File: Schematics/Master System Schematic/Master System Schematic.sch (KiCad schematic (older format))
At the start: 39 parts, among them J1 ChargerHVConn, J2 ChargerLVConn, J3 GND, J5 TS+, J6 TS-, M1 Cooling Pump, SW1 SideMounted (BRB), SW10 SMD, SW11 BRAKE_SWITCH, SW12 SW_SPST_Pressure, SW13 SW_SPST_Pressure, SW14 TOGGLE_SWITCH, SW2 SideMounted (BRB), SW3 GLVMS, SW4 Brake Over-Travel Switch, SW5 Latching Circuit Reset, SW6 Cockpit Shutdown (BRB), SW7 TSMS, SW8 SMD, SW9 HVD, U1 FuseBox_PSZACCEPS052H, U2 Bender_Isometer_IR155-3204, U3 RinehartPM100DX_MotorControll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, U4 Emrax228HV_Motor

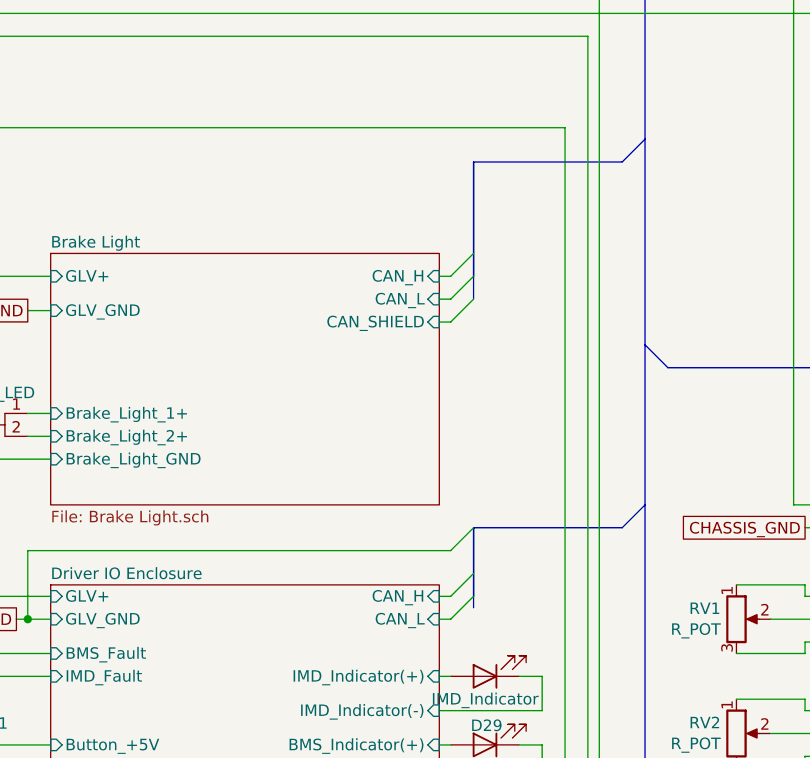
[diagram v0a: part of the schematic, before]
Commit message: Added CAN Shield Label
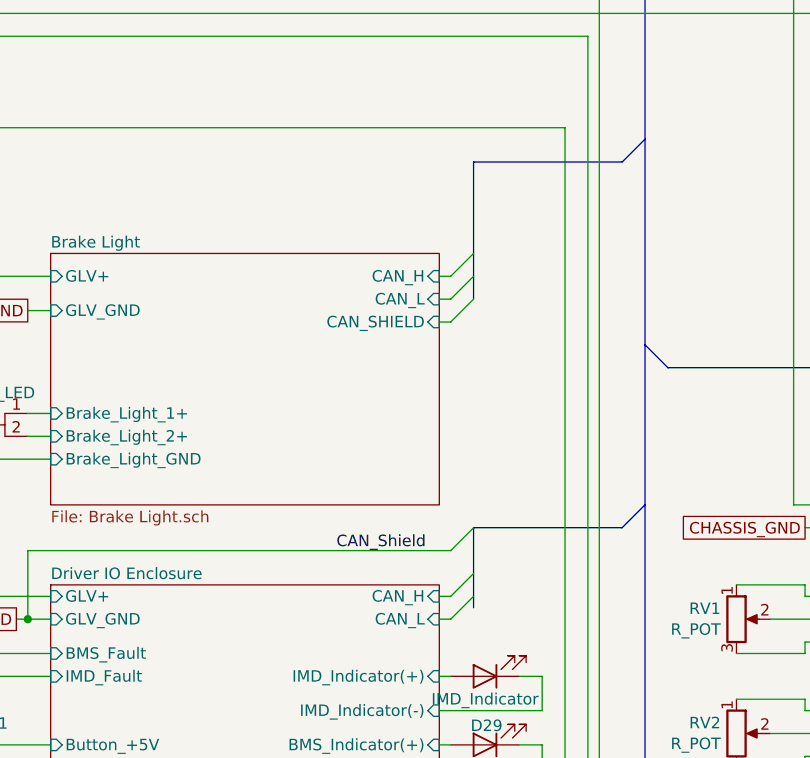
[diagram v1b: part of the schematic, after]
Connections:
- new net: U1.6, U3.23 (CANB_H), U3.8 (Reverse_Enable_Switch)
- new net: U3.~ (TS-), U4.~ (AC3) (x2)
- now unconnected: U3.23 (CANB_H), U3.8 (Reverse_Enable_Switch)
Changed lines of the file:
@@
 EESchema Schematic File Version 4
+LIBS:Master System Schematic-cache
 EELAYER 30 0
 EELAYER END
@@
 Wire Wire Line
 	7900 9400 8200 9400
-Wire Bus Line
-	11300 1650 11300 2150
+Text Label 10700 3350 0    50   ~ 0
+CAN_Shield
+Wire Bus Line
+	14550 2550 14550 3150
+Wire Bus Line
+	11650 6600 11650 6800
 Wire Bus Line
 	11300 3250 11300 3600
 Wire Bus Line
-	14550 2550 14550 3150
-Wire Bus Line
-	11650 6600 11650 6800
-Wire Bus Line
-	11300 3250 11300 3550
-Wire Bus Line
 	11300 1650 11300 2250

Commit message: Rotated first section of GLV
Increased sheet size (May still downsize back to C)
Moved GLV from CHS GND to fusebox
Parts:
- removed SW1: SideMounted (BRB), symbol Switch:SW_Push_Open
- added SW3: Side BRB, symbol Switch:SW_Push_Open
- added U1: FuseBox_PSZACCEPS052H, symbol NER:FuseBox_PSZACCEPS052H
- BT1: value 12V GLV Battery -> GLV Battery; Voltage (none) -> 12V
- CB1: value GLV Main Breaker [30A] -> GLV Main Breaker; Current (none) -> 30A
- SW2: value SideMounted (BRB) -> Side BRB
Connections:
- net CoolingPumpPower: now also SW3.2 (B); no longer SW3.1 (A)
- net at SW2.1 (A): now also SW3.1 (A)
- net at CB1.1: now also SW3.1 (A); no longer SW3.2 (B)
- new net: U1.6, U3.23 (CANB_H), U3.8 (Reverse_Enable_Switch)
- new net: U3.~ (TS-), U4.~ (AC3) (x2)
- new net: SW3.2 (B), U1.0
- now unconnected: U3.23 (CANB_H), U3.8 (Reverse_Enable_Switch)
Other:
- moved on the sheet: D29, D3, D30, D4, D5, D6, J1, J2, J3, J5, J6, LS1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

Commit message: Created Fan Banks and Moved Latching
Created the accumulator cooling fan banks in schematic
Began moving the latching circuits
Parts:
- added J?: Bank 2 Power, symbol NER:2-Pos_Generic
- added J?: Bank 1 Power, symbol NER:2-Pos_Generic
- added J?: PWM, symbol NER:2-Pos_Generic
- added M? (x8): Fan_4pin, symbol Motor:Fan_4pin
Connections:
- wire segments 276 -> 338
- no-connect marks 0 -> 8
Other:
- moved on the sheet: D29, D3, D30, D4, D5, D6, J1, J2, J3, J5, J6, LS1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

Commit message: Reducing schematic to blocks
Stripped down everything to just the heirarchical sheets and their respective master sheet components
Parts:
- removed SW11: BRAKE_SWITCH, symbol Switch:SW_SPST
- removed U1: FuseBox_PSZACCEPS052H, symbol NER:FuseBox_PSZACCEPS052H
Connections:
- net labels removed: AccumulatorFans, MotorControllerAIRControl, PC_Link
- wire segments 338 -> 236
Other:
- moved on the sheet: D29, D30, D5, D6, J1, J2, J3, J5, J6, LS1, M1, R1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

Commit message: Laid out blocks tentatively
Generally placed heirarchical sheets. Will be moved as wires are placed
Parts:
- removed RV3: BRAKE_POT, symbol Device:R_POT
- removed RV4: ACCEL_POT, symbol Device:R_POT
- D3: value SSOK2 -> SSOK
- D4: value SSOK1 -> SSOK
- SW6: value Cockpit Shutdown (BRB) -> Cockpit BRB
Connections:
- wire segments 236 -> 219
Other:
- moved on the sheet: D29, D30, D5, D6, J1, J2, J3, J5, J6, J?, LS1, M1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

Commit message: Cleaned up CAN boxes
Includes Brake Light, Pedalbox, Driver IO
Fixed spacings, sizing, layout, etc
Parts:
- D29: value IMD_Indicator -> IMD Indicator
- D30: value BMS_Indicator -> BMS Indicator
- SW14: value TOGGLE_SWITCH -> Reverse Toggle
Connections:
- wire segments 219 -> 233
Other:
- moved on the sheet: SW12, SW13
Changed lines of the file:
@@
 L Switch:SW_SPST_Temperature SW12
 U 1 1 5F6E407C
-P 17400 2350
-F 0 "SW12" H 17400 2665 50  0000 C CNN
-F 1 "SW_SPST_Pressure" H 17400 2574 50  0000 C CNN
-F 2 "" H 17400 2350 50  0001 C CNN
-F 3 "~" H 17400 2350 50  0001 C CNN
-	1    17400 2350
+P 17350 1750
+F 0 "SW12" H 17350 2065 50  0000 C CNN
+F 1 "SW_SPST_Pressure" H 17350 1974 50  0000 C CNN
+F 2 "" H 17350 1750 50  0001 C CNN
+F 3 "~" H 17350 1750 50  0001 C CNN
+	1    17350 1750
 	1    0    0    -1
 $EndComp
@@
 L Switch:SW_SPST_Temperature SW13
 U 1 1 5F6E49B5
-P 17400 2850
-F 0 "SW13" H 17400 3165 50  0000 C CNN
-F 1 "SW_SPST_Pressure" H 17400 3074 50  0000 C CNN
-F 2 "" H 17400 2850 50  0001 C CNN
-F 3 "~" H 17400 2850 50  0001 C CNN
-	1    17400 2850
-	1    0    0    -1
-$EndComp
-Wire Wire Line
-	16950 2350 17200 2350
-Wire Wire Line
-	17600 2350 17600 2450
-Wire Wire Line
-	17600 2450 16950 2450
-Wire Wire Line
-	16950 2850 17200 2850
-Wire Wire Line
-	17600 2850 17600 2950
-Wire Wire Line
-	17600 2950 16950 2950
+P 17350 2250
+F 0 "SW13" H 17350 2565 50  0000 C CNN
+F 1 "SW_SPST_Pressure" H 17350 2474 50  0000 C CNN
+F 2 "" H 17350 2250 50  0001 C CNN
+F 3 "~" H 17350 2250 50  0001 C CNN
+	1    17350 2250
+	1    0    0    -1
+$EndComp
 $Sheet
 S 15500 1650 1450 1400
@@
 F2 "GLV+" I L 15500 2950 50
 F3 "GLV_GND" I L 15500 2800 50
-F4 "CAN_L" I R 16950 1900 50
-F5 "CAN_H" I R 16950 1800 50
-F6 "Switch_Input1" I R 16950 2350 50
-F7 "Switch_Input2" I R 16950 2850 50
-F8 "Switch2-" I R 16950 2950 50
-F9 "Switch1-" I R 16950 2450 50
+F4 "CAN_L" I R 16950 2700 50
+F5 "CAN_H" I R 16950 2800 50
+F6 "Switch_Input1" I R 16950 1750 50
+F7 "Switch_Input2" I R 16950 2250 50
+F8 "Switch2-" I R 16950 2350 50
+F9 "Switch1-" I R 16950 1850 50
 F10 "POT1+" I L 15500 1750 50
 F11 "POT2+" I L 15500 2250 50
@@
 Wire Wire Line
 	19950 2650 19450 2650
-$Comp
-L Device:Speaker LS1
-U 1 1 5F9B2999
-P 21800 3050
-F 0 "LS1" H 21700 2800 50  0000 L CNN
-F 1 "Speaker" H 21650 2700 50  0000 L CNN
-F 2 "" H 21800 2850 50  0001 C CNN
-F 3 "~" H 21790 3000 50  0001 C CNN
-	1    21800 3050
-	1    0    0    -1
-$EndComp
 $Sheet
 S 20000 9150 1750 2200
@@
 	27150 9650 28150 9650
 Wire Wire Line
-	18350 3000 18400 3000
-Wire Wire Line
-	18350 3100 18400 3100
-Entry Wire Line
-	18400 3100 18500 3000
-Entry Wire Line
-	18400 3000 18500 2900
-Wire Wire Line
-	21450 1400 21500 1400
-Wire Wire Line
-	21450 1500 21500 1500
-Entry Wire Line
-	21500 1500 21600 1400
-Entry Wire Line
-	21500 1400 21600 1300
+	16950 2800 17000 2800
+Wire Wire Line
+	16950 2700 17000 2700
+Entry Wire Line
+	17000 2700 17100 2800
+Entry Wire Line
+	17000 2800 17100 2900
+Wire Wire Line
+	21450 3100 21500 3100
+Wire Wire Line
+	21450 3000 21500 3000
+Entry Wire Line
+	21500 3000 21600 3100
+Entry Wire Line
+	21500 3100 21600 3200
 Text GLabel 11650 2500 0    50   UnSpc ~ 0
 CHASSIS_GND
-Text GLabel 19900 1500 0    50   UnSpc ~ 0
+Text GLabel 19850 3100 0    50   UnSpc ~ 0
 CHASSIS_GND
 Wire Wire Line
@@
 	17150 17000 17150 18050
 Wire Wire Line
-	21450 3150 21600 3150
-Wire Wire Line
-	21450 3050 21600 3050
+	21450 1500 21600 1500
+Wire Wire Line
+	21450 1400 21600 1400
 Wire Wire Line
 	12900 2600 12950 2600
@@
 Entry Wire Line
 	30350 7250 30450 7150
-$Comp
-L Device:LED D29
-U 1 1 5F986518
-P 21750 1750
-F 0 "D29" H 21743 1966 50  0000 C CNN
-F 1 "IMD_Indicator" H 21750 1850 50  0000 C CNN
-F 2 "" H 21750 1750 50  0001 C CNN
-F 3 "https://www.mouser.com/datasheet/2/26/apem_03162018_Q14_Series_HMI_2017-1730666.pdf" H 21750 1750 50  0001 C CNN
-	1    21750 1750
-	-1   0    0    1
-$EndComp
-$Comp
-L Device:LED D30
-U 1 1 5F9AD83A
-P 21750 2350
-F 0 "D30" H 21743 2566 50  0000 C CNN
-F 1 "BMS_Indicator" H 21750 2450 50  0000 C CNN
-F 2 "" H 21750 2350 50  0001 C CNN
-F 3 "https://www.mouser.com/datasheet/2/26/apem_03162018_Q14_Series_HMI_2017-1730666.pdf" H 21750 2350 50  0001 C CNN
-	1    21750 2350
-	-1   0    0    1
-$EndComp
-Wire Wire Line
-	21450 1750 21500 1750
-Wire Wire Line
-	21900 1750 22000 1750
-Wire Wire Line
-	22000 1750 22000 1900
-Wire Wire Line
-	21900 2000 21450 2000
-Wire Wire Line
-	21450 2050 21500 2050
-Wire Wire Line
-	21900 2350 22000 2350
-Wire Wire Line
-	22000 2350 22000 2500
-Wire Wire Line
-	21900 2500 21450 2500
-$Comp
-L Switch:SW_SPST SW14
-U 1 1 5FA01B38
-P 21700 2650
-F 0 "SW14" H 21700 2450 50  0000 C CNN
-F 1 "TOGGLE_SWITCH" H 21700 2550 50  0000 C CNN
-F 2 "" H 21700 2650 50  0001 C CNN
-F 3 "~" H 21700 2650 50  0001 C CNN
-	1    21700 2650
-	1    0    0    -1
-$EndComp
-Wire Wire Line
-	21450 2350 21500 2350
-Wire Wire Line
-	21900 2650 21900 2850
-Wire Wire Line
-	21900 2850 21450 2850
 Wire Wire Line
 	17400 16900 17500 16900
@@
 Text Label 5900 7700 3    50   ~ 0
 CoolingPumpPower
-Wire Wire Line
-	19900 1500 19950 1500
 $Sheet
 S 13200 9150 1750 1200
@@
 F0 "Driver IO Enclosure" 50
 F1 "Driver IO Enclosure.sch" 50
-F2 "CAN_L" I R 21450 1500 50
-F3 "CAN_H" I R 21450 1400 50
-F4 "GLV+" I L 20050 1400 50
-F5 "GLV_GND" I L 20050 1500 50
+F2 "CAN_L" I R 21450 3100 50
+F3 "CAN_H" I R 21450 3000 50
+F4 "GLV+" I L 20050 2950 50
+F5 "GLV_GND" I L 20050 3100 50
 F6 "LED(+)" I L 20050 2450 50
 F7 "Button_GND" I L 20050 2650 50
 F8 "Button_Input" I L 20050 2750 50
 F9 "Button_+5V" I L 20050 2050 50
-F10 "Speaker+" I R 21450 2750 50
-F11 "Speaker-" I R 21450 2850 50
-F12 "StartEnable" I L 20050 2850 50
-F13 "IMD_Indicator(+)" I R 21450 1750 50
-F14 "IMD_Indicator(-)" I R 21450 1900 50
-F15 "BMS_Indicator(+)" I R 21450 2050 50
-F16 "BMS_Indicator(-)" I R 21450 2200 50
-F17 "Toggle(+)" I R 21450 2350 50
-F18 "Toggle(-)" I R 21450 2550 50
-F19 "BMS_Fault" I L 20050 1650 50
-F20 "IMD_Fault" I L 20050 1750 50
+F10 "Speaker+" I R 21450 1400 50
+F11 "Speaker-" I R 21450 1500 50
+F12 "StartEnable" I L 20050 1400 50
+F13 "IMD_Indicator(+)" I R 21450 1900 50
+F14 "IMD_Indicator(-)" I R 21450 2000 50
+F15 "BMS_Indicator(+)" I R 21450 2350 50
+F16 "BMS_Indicator(-)" I R 21450 2450 50
+F17 "Toggle(+)" I R 21450 2750 50
+F18 "Toggle(-)" I R 21450 2850 50
+F19 "BMS_Fault" I L 20050 1550 50
+F20 "IMD_Fault" I L 20050 1650 50
 $EndSheet
 Entry Wire Line
-	21500 1200 21600 1100
+	21500 3400 21600 3500
 Entry Wire Line
 	13050 2600 12950 2500
@@
 	12950 2500 12900 2500
 Wire Wire Line
-	19950 1500 19950 1200
-Connection ~ 19950 1500
-Wire Wire Line
-	19950 1500 20050 1500
-Wire Wire Line
-	21500 1200 19950 1200
+	21500 3400 19950 3400
 Wire Notes Line
 	19600 17000 17150 17000
@@
 Wire Wire Line
 	22150 17300 22450 17300
-Text Label 21000 1200 0    50   ~ 0
+Text Label 21300 3400 2    50   ~ 0
 CAN_Shield
 $Comp
@@
 $EndSheet
 Wire Wire Line
-	11750 2700 8000 2700
-Wire Wire Line
-	8000 2700 8000 7000
-Wire Wire Line
 	15500 1900 15350 1900
 Wire Wire Line
@@
 Wire Wire Line
 	15500 2800 15400 2800
-Wire Bus Line
-	18500 2400 18500 3000
+Wire Wire Line
+	16950 2250 17150 2250
+Wire Wire Line
+	17550 2250 17600 2250
+Wire Wire Line
+	17600 2250 17600 2350
+Wire Wire Line
+	17600 2350 16950 2350
+Wire Wire Line
+	16950 1750 17150 1750
+Wire Wire Line
+	17550 1750 17600 1750
+Wire Wire Line
+	17600 1750 17600 1850
+Wire Wire Line
+	17600 1850 16950 1850
+Wire Wire Line
+	16950 2900 17000 2900
+Entry Wire Line
+	17000 2900 17100 3000
+Wire Wire Line
+	11750 2700 11500 2700
+Wire Wire Line
+	11500 2700 11500 4200
+Wire Wire Line
+	11500 4200 8000 4200
+Wire Wire Line
+	8000 4200 8000 7000
+Wire Wire Line
+	15500 2950 15250 2950
+Wire Wire Line
+	15250 2950 15250 4350
+Wire Wire Line
+	15250 4350 8150 4350
+Wire Wire Line
+	8150 4350 8150 7000
+$Comp
+L Device:LED D29
+U 1 1 61F2ACEE
+P 21750 1900
+F 0 "D29" H 21743 1645 50  0000 C CNN
+F 1 "IMD Indicator" H 21743 1736 50  0000 C CNN
+F 2 "" H 21750 1900 50  0001 C CNN
+F 3 "~" H 21750 1900 50  0001 C CNN
+	1    21750 1900
+	-1   0    0    1
+$EndComp
+$Comp
+L Device:LED D30
+U 1 1 61F2CBDA
+P 21750 2350
+F 0 "D30" H 21743 2095 50  0000 C CNN
+F 1 "BMS Indicator" H 21743 2186 50  0000 C CNN
+F 2 "" H 21750 2350 50  0001 C CNN
+F 3 "~" H 21750 2350 50  0001 C CNN
+	1    21750 2350
+	-1   0    0    1
+$EndComp
+$Comp
+L Switch:SW_SPST SW14
+U 1 1 61F4E8CC
+P 21750 2750
+F 0 "SW14" H 21750 2985 50  0000 C CNN
+F 1 "Reverse Toggle" H 21750 2894 50  0000 C CNN
+F 2 "" H 21750 2750 50  0001 C CNN
+F 3 "~" H 21750 2750 50  0001 C CNN
+	1    21750 2750
+	1    0    0    -1
+$EndComp
+Connection ~ 19950 3100
+Wire Wire Line
+	19950 3100 20050 3100
+Wire Wire Line
+	19850 3100 19950 3100
+$Comp
+L Device:Speaker LS1
+U 1 1 620AED7F
+P 21800 1400
+F 0 "LS1" H 21970 1396 50  0000 L CNN
+F 1 "Speaker" H 21970 1305 50  0000 L CNN
+F 2 "" H 21800 1200 50  0001 C CNN
+F 3 "~" H 21790 1350 50  0001 C CNN
+	1    21800 1400
+	1    0    0    -1
+$EndComp
+Wire Wire Line
+	21450 1900 21600 1900
+Wire Wire Line
+	22000 1900 22000 2000
+Wire Wire Line
+	22000 2000 21450 2000
+Wire Wire Line
+	21900 1900 22000 1900
+Wire Wire Line
+	21450 2350 21600 2350
+Wire Wire Line
+	21900 2350 22000 2350
+Wire Wire Line
+	22000 2350 22000 2450
+Wire Wire Line
+	22000 2450 21450 2450
+Wire Wire Line
+	21450 2750 21550 2750
+Wire Wire Line
+	21950 2750 22050 2750
+Wire Wire Line
+	22050 2750 22050 2850
+Wire Wire Line
+	22050 2850 21450 2850
+Wire Wire Line
+	19950 3100 19950 3400
+Wire Wire Line
+	20050 2950 19200 2950
+Wire Wire Line
+	19200 4500 8300 4500
+Wire Wire Line
+	8300 4500 8300 7000
+Wire Wire Line
+	19200 2950 19200 4500
 Wire Bus Line
 	30450 7150 30450 7350
 Wire Bus Line
-	21600 1100 21600 1450
+	21600 3100 21600 3450
 Wire Bus Line
 	13050 2600 13050 3200
+Wire Bus Line
+	17100 2800 17100 3400
 $EndSCHEMATC

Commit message: Shifting shutdown circuit a bit
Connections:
- wire segments 233 -> 254
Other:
- moved on the sheet: J3, J5, J6, R1, SW4, SW5, SW6, SW7, U2

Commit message: IMD Container
Added IMD into a container
Wired the IMD
+ Some extra bits
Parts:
- removed R1: 2.2k, symbol Device:R
- removed U2: Bender_Isometer_IR155-3204, symbol NER:Bender_Isometer_IR155-3204
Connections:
- wire segments 254 -> 253
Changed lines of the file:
@@
 $Descr D 34000 22000
 encoding utf-8
-Sheet 1 21
+Sheet 1 22
 Title "NER FH 2020-2021 Master Electrical Schematic"
 Date "2020-10-29"
@@
 Text GLabel 2950 7600 0    50   UnSpc ~ 0
 CHASSIS_GND
-$Comp
-L NER:Bender_Isometer_IR155-3204 U2
-U 1 1 5F94A015
-P 16200 11200
-F 0 "U2" H 16200 11315 50  0000 C CNN
-F 1 "Bender_Isometer_IR155-3204" H 16200 11224 50  0000 C CNN
-F 2 "" H 16200 11200 50  0001 C CNN
-F 3 "" H 16200 11200 50  0001 C CNN
-	1    16200 11200
-	-1   0    0    -1
-$EndComp
-Text GLabel 15350 11550 0    50   UnSpc ~ 0
-CHASSIS_GND
-$Comp
-L Device:R R1
-U 1 1 5F4E06AE
-P 16200 10900
-F 0 "R1" V 16407 10900 50  0000 C CNN
-F 1 "2.2k" V 16316 10900 50  0000 C CNN
-F 2 "" V 16130 10900 50  0001 C CNN
-F 3 "~" H 16200 10900 50  0001 C CNN
-	1    16200 10900
-	0    -1   -1   0
-$EndComp
-Wire Wire Line
-	15350 11550 15450 11550
-Wire Wire Line
-	15500 11450 15450 11450
-Wire Wire Line
-	15450 11450 15450 11550
-Connection ~ 15450 11550
-Wire Wire Line
-	15450 11550 15500 11550
-Wire Wire Line
-	15450 11550 15450 11650
-Wire Wire Line
-	15450 11650 15500 11650
-Wire Wire Line
-	15450 11450 15450 10900
-Wire Wire Line
-	15450 10900 16050 10900
-Connection ~ 15450 11450
 $Comp
 L Connector:Conn_01x01_Female J6
@@
 F8 "GND" O R 23150 17500 50
 $EndSheet
-Wire Wire Line
-	17150 11650 16900 11650
-Wire Wire Line
-	16900 11550 17200 11550
 Text GLabel 11700 14250 2    50   UnSpc ~ 0
 CHASSIS_GND
-Wire Wire Line
-	16350 10900 17200 10900
-Wire Wire Line
-	17200 10900 17200 11350
-Wire Wire Line
-	17200 11350 16900 11350
 $Comp
 L Device:LED D5
@@
 Wire Wire Line
 	13700 9200 14400 9200
-Wire Wire Line
-	18150 9200 18850 9200
 Connection ~ 18850 9200
 Wire Wire Line
@@
 Wire Wire Line
 	12750 7050 18750 7050
+$Sheet
+S 15300 10200 950  450
+U 626EC638
+F0 "IMD Container" 50
+F1 "IMD_Container.sch" 50
+F2 "HV_Sense+" B R 16250 10250 50
+F3 "HV_Sense-" B R 16250 10350 50
+F4 "GLV" I L 15300 10600 50
+F5 "GND2" U L 15300 10450 50
+F6 "GND1" U L 15300 10350 50
+F7 "GND" U L 15300 10250 50
+$EndSheet
+Text GLabel 15150 10250 0    50   UnSpc ~ 0
+CHASSIS_GND
+Wire Wire Line
+	15150 10250 15300 10250
+Text GLabel 15150 10350 0    50   UnSpc ~ 0
+CHASSIS_GND
+Wire Wire Line
+	15150 10350 15300 10350
+Text GLabel 15150 10450 0    50   UnSpc ~ 0
+CHASSIS_GND
+Wire Wire Line
+	15150 10450 15300 10450
+Wire Wire Line
+	8300 10600 8300 8200
+Wire Wire Line
+	8300 10600 15300 10600
+Wire Wire Line
+	16250 10250 16600 10250
+Wire Wire Line
+	16600 10250 16600 9350
+Wire Wire Line
+	16600 9350 20000 9350
+Wire Wire Line
+	20000 9450 16700 9450
+Wire Wire Line
+	16700 9450 16700 10350
+Wire Wire Line
+	16700 10350 16250 10350
+Wire Wire Line
+	15500 9200 18850 9200
+Wire Wire Line
+	21750 9200 21900 9200
 Wire Bus Line
 	30450 7150 30450 7350
@@
 Wire Bus Line
 	17100 2800 17100 3400
+Text GLabel 21900 9200 2    50   UnSpc ~ 0
+CHASSIS_GND
 $EndSCHEMATC
